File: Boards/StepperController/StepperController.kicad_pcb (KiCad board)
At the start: 2 copper layers, 160 x 100 mm, 167 parts, among them IC1 ATMEGA645A-A, J1 I2C, J2 SPI_Extern, J3 ISP, J4 Reference, J5 Display, J7 Spindle, P1 Power, P10 CONN_Z, P2 Cover, P3 USB_B, P4 Relay2, P5 Relay1, P6 Emer_Off, P8 CONN_X, P9 CONN_Y, Q1 BC817-40, Q2 BC817-40, Q3 BC817-40, Q4 BC817-40, Q5 BC817-40, SW2 SW_1, SW3 SW_2, U1 LM2595S-5, U2 74LS11, U3 FT232RL, U5 TMC2660, U6 TMC2660, U7 TMC2660, U8 74HC00, X1 16MHz, Y1 20MHz

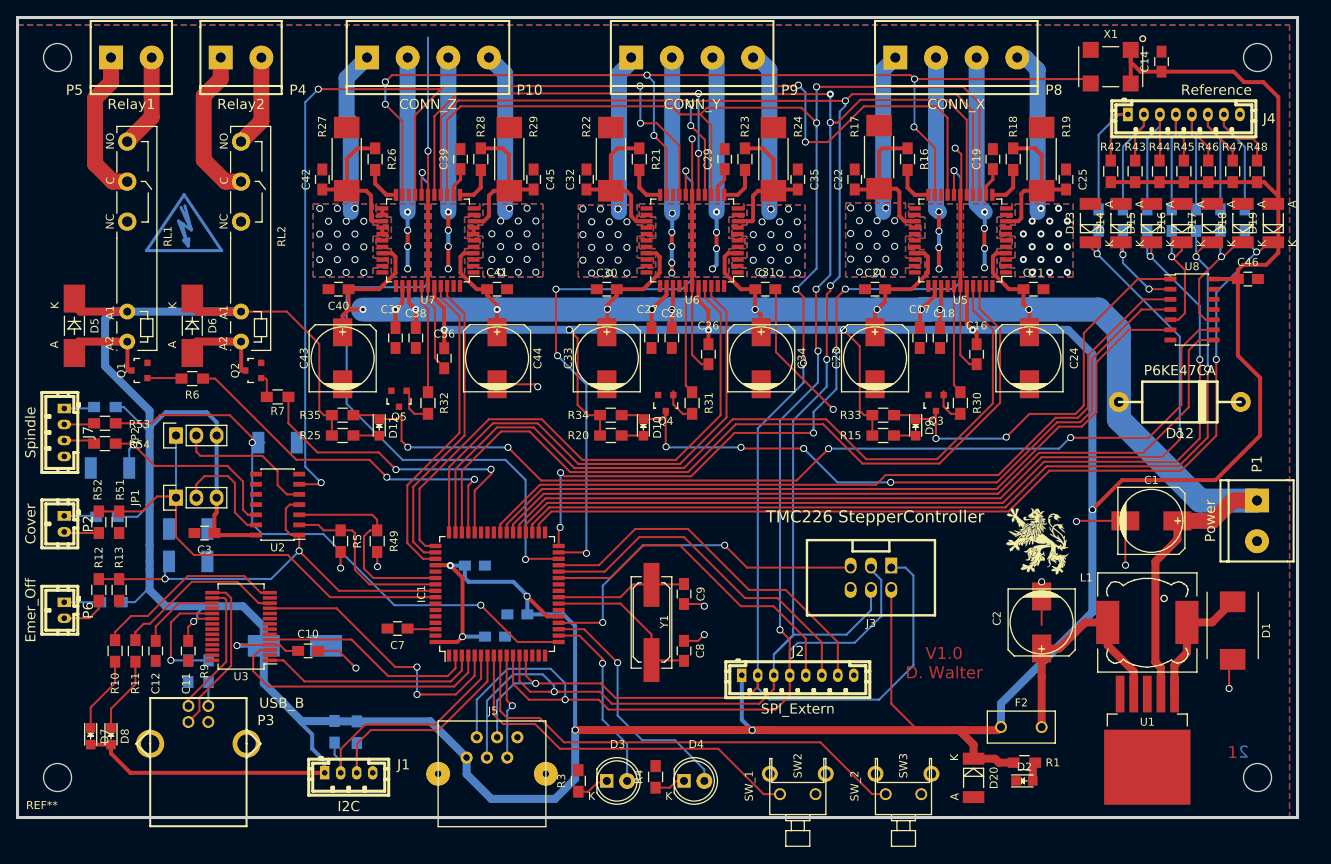
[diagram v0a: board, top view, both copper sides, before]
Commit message: Thermal vias, changed footprint of logic ics
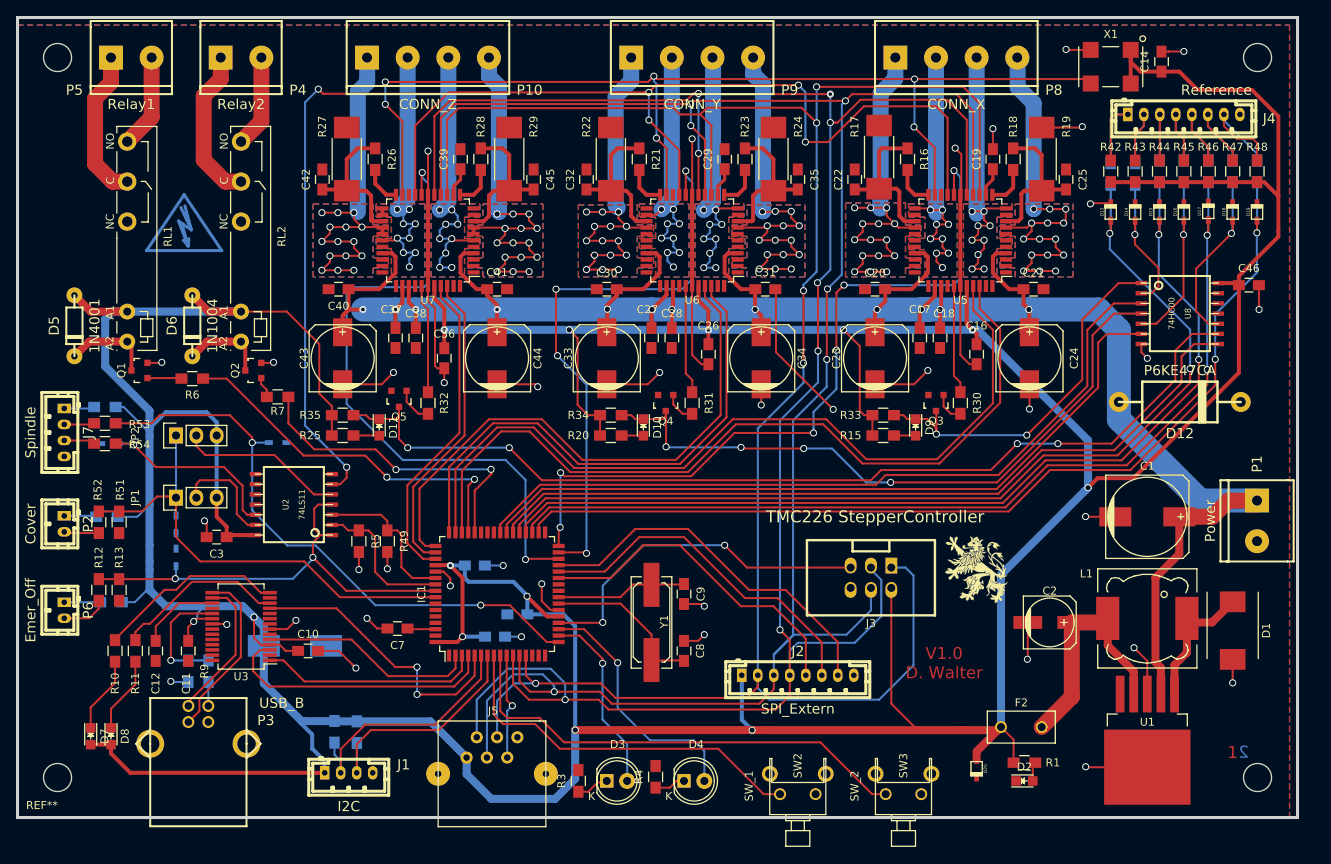
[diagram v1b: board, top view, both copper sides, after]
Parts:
- C1: footprint Capacitors_SMD:c_elec_8x10.5 -> Capacitors_SMD:c_elec_10x10.5
- C2: footprint Capacitors_SMD:c_elec_8x10.5 -> Capacitors_SMD:c_elec_6.3x5.7
- D13, D14, D15, D16, D17, D18, D19, D20, D21, D22, D23, D29: footprint Diodes_SMD:MELF_Standard -> w_smd_diode:sod323
- D5, D6: footprint Diodes_SMD:MELF_Handsoldering -> w_pth_diodes:diode_do35
- U2, U8: footprint Housings_SOIC:SOIC-14_3.9x8.7mm_Pitch1.27mm -> w_smd_dil:soic-14
- moved G*** 8.41 mm to (183.9, 121.9)
- moved R37 6.28 mm to (206.8, 72.1)
- moved R38 6.28 mm to (209.8, 72.1)
- moved R39 6.28 mm to (212.9, 72.1)
- moved R40 6.28 mm to (215.9, 72.1)
- moved R41 6.28 mm to (218.9, 72.1)
- moved R2 5.96 mm to (200.7, 72.5)
- moved R36 5.96 mm to (203.7, 72.5)
- moved D23 3.05 mm to (75.6, 106.2)
- moved D13 2.89 mm to (200.7, 77.2)
- moved D19 2.46 mm to (218.9, 77.2)
- moved R5 2.29 mm to (106.7, 118.4)
- moved D14 2.25 mm to (203.7, 77.2)
- moved U2 2.03 mm to (98.6, 113.8), turned to 90 degrees
- moved D18 1.88 mm to (215.9, 77.2)
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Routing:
- net /Controller/Stall_Z: track 15.7 -> 125.5 mm, vias 0 -> 4
- net GND: track 270.5 -> 231.2 mm, vias 18 -> 39
- net /Driver/Driver_Z/OA1_Z: track 21.0 -> 53.5 mm, vias 1 -> 15
- net /Driver/Driver_Y/OA1_Y: track 19.9 -> 52.0 mm, vias 1 -> 15
- net /Driver/Driver_X/OB1_X: track 20.2 -> 52.0 mm, vias 1 -> 15
- net /Driver/Driver_X/OA1_X: track 21.0 -> 52.3 mm, vias 1 -> 15
- net /Driver/Driver_Y/OB1_Y: track 20.6 -> 52.0 mm, vias 1 -> 15
- net /Driver/Driver_Z/OB1_Z: track 21.4 -> 52.0 mm, vias 1 -> 15
- net +5V: track 737.8 -> 715.2 mm
- net /Driver/Driver_Z/OA2_Z: track 26.4 -> 36.7 mm, vias 4 -> 9
- net /Driver/Driver_X/OA2_X: track 26.7 -> 36.9 mm, vias 4 -> 9
- net /Driver/Driver_Y/OA2_Y: track 26.6 -> 36.7 mm, vias 4 -> 9
- net /Driver/Driver_Z/OB2_Z: track 27.2 -> 36.7 mm, vias 4 -> 9
- net /Driver/Driver_X/OB2_X: track 26.6 -> 35.9 mm, vias 4 -> 9
- net /Driver/Driver_Y/OB2_Y: track 27.0 -> 36.2 mm, vias 5 -> 9
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
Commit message: Work in Progress
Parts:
- removed U8: 74HC00, w_smd_dil:soic-14
- added U4: 74HC08, w_smd_dil:so-14, F.Cu at (210.8, 89.9)
- C1: value 220µF -> 100µF; footprint Capacitors_SMD:c_elec_10x10.5 -> Capacitors_SMD:c_elec_8x10.5
- C2: value 100µF -> 1000µF; footprint Capacitors_SMD:c_elec_6.3x5.7 -> Capacitors_ThroughHole:C_Radial_D16_L25_P7.5
- D1: value MBRS240 -> SK34; footprint Diodes_SMD:DO-214AB -> w_smd_diode:do214ac
- D12: value P6KE47CA -> SM6T 39A; footprint w_pth_diodes:diode_do201 -> w_smd_diode:do214aa
- D13, D14, D16, D17, D18, D19: footprint w_smd_diode:sod323 -> w_smd_trans:sot23
- D15: value 5V -> ZMY5,6; footprint w_smd_diode:sod323 -> w_smd_trans:sot23
- D20: value 6V -> P6SMB 6,8A; footprint w_smd_diode:sod323 -> w_smd_diode:do214aa
- D21, D22, D23, D29: footprint w_smd_diode:sod323 -> w_smd_trans:sot23; moved to F.Cu
- D5: value 1N4001 -> 1N4148; footprint w_pth_diodes:diode_do35 -> w_smd_diode:sod323
- D6: value 1N1004 -> 1N4148; footprint w_pth_diodes:diode_do35 -> w_smd_diode:sod323
- U1: value LM2595S-5 -> LM2576S-5
- U2: value 74LS11 -> 74HC11; footprint w_smd_dil:soic-14 -> w_smd_dil:so-14
- moved G*** 34.6 mm to (149.4, 124.2)
- moved D22 22.3 mm to (74.9, 100.6), turned to 180 degrees
- moved C1 17.8 mm to (217.4, 128.3), turned to 180 degrees
- moved D12 14.7 mm to (210.8, 115.6), turned to 90 degrees
- moved D1 14.4 mm to (205.2, 119.9), turned to 180 degrees
- moved D2 8.19 mm to (182.4, 145.0), turned to 180 degrees
- moved R1 8.12 mm to (182.5, 142.7), turned to 180 degrees
- moved D20 7.41 mm to (190.8, 144.0), turned to 0 degrees
- moved C14 7.28 mm to (200.7, 54.9), turned to 180 degrees
- moved C8 4.68 mm to (142.7, 131.1)
- moved C9 4.64 mm to (142.7, 124.2)
- moved D23 4.61 mm to (79.4, 108.7)
- moved D29 4.47 mm to (79.4, 117.1), turned to 180 degrees
- moved C5 4.43 mm to (119.4, 129.3), turned to 90 degrees
- moved Y1 4.38 mm to (138.9, 127.8)
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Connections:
- C1 pad 1: /Driver/Sup_36V -> VSA
- C17 pad 1: /Driver/Sup_36V -> VSA
- C17 pad 2: GND -> Net-(C17-Pad2)
- C18 pad 1: /Driver/Sup_36V -> VSA
- C20 pad 1: /Driver/Sup_36V -> VSA
- C21 pad 1: /Driver/Sup_36V -> VSA
- C23 pad 1: /Driver/Sup_36V -> VSA
- C24 pad 1: /Driver/Sup_36V -> VSA
- C27 pad 1: /Driver/Sup_36V -> VSA
- C27 pad 2: GND -> Net-(C27-Pad2)
- C28 pad 1: /Driver/Sup_36V -> VSA
- C30 pad 1: /Driver/Sup_36V -> VSA
- C31 pad 1: /Driver/Sup_36V -> VSA
- C33 pad 1: /Driver/Sup_36V -> VSA
- C34 pad 1: /Driver/Sup_36V -> VSA
- C37 pad 1: /Driver/Sup_36V -> VSA
- C37 pad 2: GND -> Net-(C37-Pad2)
- C38 pad 1: /Driver/Sup_36V -> VSA
- C40 pad 1: /Driver/Sup_36V -> VSA
- C41 pad 1: /Driver/Sup_36V -> VSA
- C43 pad 1: /Driver/Sup_36V -> VSA
- C44 pad 1: /Driver/Sup_36V -> VSA
- D12 pad 1: /Driver/Sup_36V -> VSA
- P1 pad 1: /Driver/Sup_36V -> VSA
- U1 pad 1: Net-(D1-Pad1) -> VSA
- U1 pad 2: /Driver/Sup_36V -> Net-(D1-Pad1)
- U5 pad 1: (no net) -> VSA
- U5 pad 30: /Driver/Sup_36V -> VSA
- U5 pad 33: (no net) -> VSA
- U5 pad 35: /Driver/Sup_36V -> Net-(C17-Pad2)
- U5 pad 36: /Driver/Sup_36V -> VSA
- U5 pad 4: /Driver/Sup_36V -> VSA
- U6 pad 1: (no net) -> VSA
- U6 pad 30: /Driver/Sup_36V -> VSA
- U6 pad 33: (no net) -> VSA
- U6 pad 35: /Driver/Sup_36V -> Net-(C27-Pad2)
- U6 pad 36: /Driver/Sup_36V -> VSA
- U6 pad 4: /Driver/Sup_36V -> VSA
- U7 pad 1: (no net) -> VSA
- U7 pad 30: /Driver/Sup_36V -> VSA
- U7 pad 33: (no net) -> VSA
- U7 pad 35: /Driver/Sup_36V -> Net-(C37-Pad2)
- U7 pad 36: /Driver/Sup_36V -> VSA
- U7 pad 4: /Driver/Sup_36V -> VSA
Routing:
- net /Driver/Sup_36V: track 295.7 -> 0.00 mm, vias 12 -> 0
- net VSA: track 0.00 -> 211.4 mm
- net /Driver/Driver_X/OA1_X: track 52.3 -> 25.1 mm, vias 15 -> 1
- net /Driver/Driver_X/BRB_X: track 20.7 -> 0.00 mm
- net /Driver/Driver_X/BRA_X: track 19.5 -> 0.00 mm
- net /Driver/Driver_X/OB1_X: track 52.0 -> 36.1 mm, vias 15 -> 6
- net GND: track 231.2 -> 218.1 mm, vias 39 -> 55
- net /Controller/Step_X: track 102.4 -> 94.5 mm
- net /Controller/Dir_X: track 102.5 -> 95.0 mm
- net Net-(D1-Pad1): track 16.4 -> 22.8 mm
- net /Controller/Rel_2: track 39.8 -> 33.4 mm
- net /Driver/Driver_X/SRB_X: track 5.18 -> 0.00 mm
- net /Driver/Driver_X/SRA_X: track 5.18 -> 0.00 mm
- net Net-(C8-Pad1): track 20.5 -> 15.5 mm
- net Net-(C2-Pad1): track 29.4 -> 34.4 mm
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- added copper zone on F.Cu, net /Driver/Driver_X/BRA_X
- added copper zone on F.Cu, net /Driver/Driver_X/BRB_X
- added copper zone on F.Cu, net /Driver/Driver_X/SRA_X
- added copper zone on F.Cu, net /Driver/Driver_X/SRB_X
- added copper zone on F.Cu, net VSA
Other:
- board text added: "Display"
- board text added: "ISP"
- board text added: "TMC2660 StepperController"
- board text removed: "TMC226 StepperController"

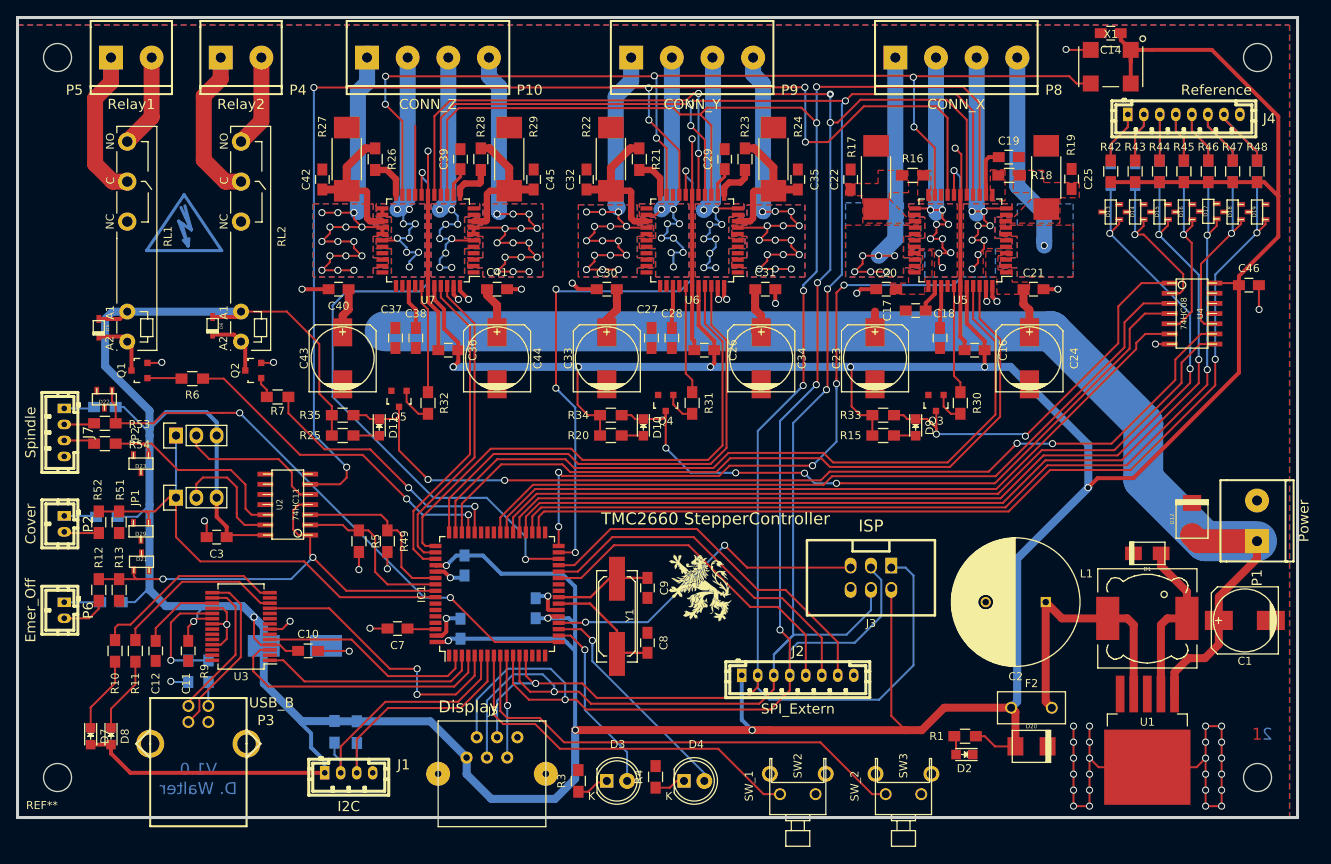
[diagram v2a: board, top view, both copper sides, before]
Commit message: Added Ext. Connector, new Layout of Supply to TMC2660
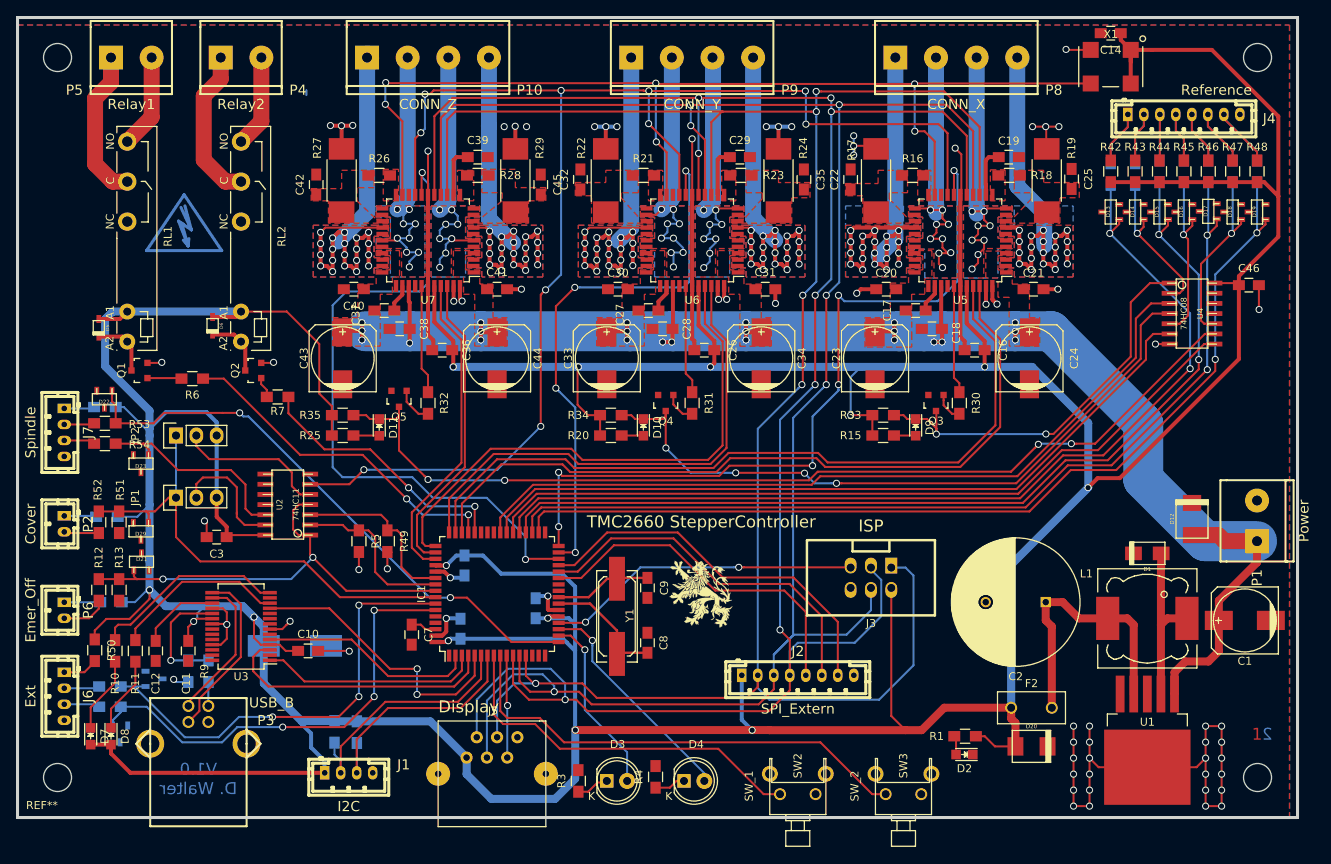
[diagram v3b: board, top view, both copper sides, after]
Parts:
- added D24: ZMY5,6, w_smd_trans:sot23, B.Cu at (81.1, 135.6)
- added D25: ZMY5,6, w_smd_trans:sot23, B.Cu at (76.8, 142.5)
- added J6: Ext, w_conn_jst-ph:b4b-ph-kl, F.Cu at (69.8, 137.7)
- added R50: 10R, Resistors_SMD:R_0805_HandSoldering, F.Cu at (73.7, 132.0)
- added R55: 10R, Resistors_SMD:R_0805_HandSoldering, B.Cu at (75.6, 136.5)
- added R60: 10R, Resistors_SMD:R_0805_HandSoldering, B.Cu at (75.6, 139.1)
- R12, R14, R52, R53, R54, R58, R59: value 100R -> 10R
- moved C37 3.70 mm to (109.9, 89.5), turned to 0 degrees
- moved C27 3.45 mm to (142.9, 89.5), turned to 0 degrees
- moved R29 2.77 mm to (126.2, 73.3)
- moved R27 2.74 mm to (104.5, 73.3)
- moved R22 2.74 mm to (137.5, 73.3)
- moved R24 2.74 mm to (159.1, 73.3)
- moved C38 2.31 mm to (111.8, 91.8), turned to 180 degrees
- moved C39 2.17 mm to (121.5, 70.4), turned to 0 degrees
- moved R21 2.09 mm to (142.2, 72.6), turned to 0 degrees
- moved R23 2.09 mm to (154.4, 72.6), turned to 180 degrees
- moved R26 2.09 mm to (109.2, 72.6), turned to 0 degrees
- moved R28 2.07 mm to (121.5, 72.6), turned to 180 degrees
- moved C7 1.93 mm to (113.3, 130.0), turned to 270 degrees
- moved C29 1.92 mm to (154.3, 70.4), turned to 0 degrees
- moved C40 1.91 mm to (106.0, 86.9)
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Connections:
- IC1 pad 58: (no net) -> /Controller/Ext1
- IC1 pad 59: (no net) -> /Controller/Ext2
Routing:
- net /Controller/Ext2: track 0.00 -> 57.2 mm, vias 0 -> 3
- net /Controller/Ext1: track 0.00 -> 57.0 mm, vias 0 -> 3
- net /Driver/Driver_X/OA1_X: track 25.1 -> 55.0 mm, vias 1 -> 20
- net /Driver/Driver_X/OB1_X: track 36.1 -> 62.9 mm, vias 6 -> 20
- net GND: track 218.1 -> 239.4 mm, vias 55 -> 68
- net /Driver/Driver_Z/BRB_Z: track 18.8 -> 0.00 mm
- net /Driver/Driver_Y/BRA_Y: track 18.8 -> 0.00 mm
- net /Driver/Driver_Y/BRB_Y: track 18.7 -> 0.00 mm
- net /Driver/Driver_Z/BRA_Z: track 18.7 -> 0.00 mm
- net +5V: track 712.8 -> 725.0 mm, vias 13 -> 14
- net /Driver/Driver_Y/OB1_Y: track 51.1 -> 61.0 mm, vias 15 -> 20
- net /Driver/Driver_Z/OB1_Z: track 52.0 -> 61.5 mm, vias 15 -> 20
- net VSA: track 211.4 -> 217.9 mm, vias 0 -> 23
- net /Driver/Driver_Z/SRA_Z: track 5.29 -> 0.00 mm
- net /Controller/CS_Z: track 79.9 -> 85.0 mm
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- added copper zone on F.Cu, net /Driver/Driver_Y/BRA_Y
- added copper zone on F.Cu, net /Driver/Driver_Y/BRB_Y
- added copper zone on F.Cu, net /Driver/Driver_Y/SRA_Y
- added copper zone on F.Cu, net /Driver/Driver_Y/SRB_Y
- added copper zone on F.Cu, net /Driver/Driver_Z/BRA_Z
- added copper zone on F.Cu, net /Driver/Driver_Z/BRB_Z
- added copper zone on F.Cu, net /Driver/Driver_Z/SRA_Z
- added copper zone on F.Cu, net /Driver/Driver_Z/SRB_Z

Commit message: Layout updated
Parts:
- added C15: 10µF, Capacitors_SMD:C_0805_HandSoldering, B.Cu at (186.1, 123.8)
- added C47: 10µF, Capacitors_SMD:C_0805_HandSoldering, B.Cu at (125.1, 123.8)
- C13: footprint Capacitors_Tantalum_SMD:TantalC_SizeD_EIA-7343_HandSoldering -> Capacitors_SMD:C_0805_HandSoldering
- D12: value SM6T 39A -> SM6T 30CA
- L1: value 100µH -> L-PISR 100µH; footprint Choke_SMD:Choke_SMD_12x12mm_h8mm -> Choke_SMD:Choke_SMD_PISR_Handsoldering_FASTRON
- moved D1 11.0 mm to (206.4, 130.8)
- moved L1 7.38 mm to (205.7, 120.7), turned to 0 degrees
- moved D8 6.32 mm to (78.1, 148.6)
- moved D7 6.11 mm to (74.9, 148.6)
- moved P1 5.97 mm to (218.9, 109.9)
- moved D12 5.74 mm to (210.8, 109.9)
- moved C14 5.46 mm to (200.7, 60.3), turned to 90 degrees
- moved X1 4.81 mm to (196.0, 60.3), turned to 90 degrees
- moved C2 3.43 mm to (189.9, 123.8)
- moved C1 3.30 mm to (216.5, 131.4)
- moved J3 3.05 mm to (167.6, 122.9)
- moved C13 2.18 mm to (96.5, 131.4)
- moved R2 0.33 mm to (200.7, 72.1)
- moved R36 0.33 mm to (203.7, 72.1)
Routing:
- net /Controller/SDO: track 257.0 -> 233.8 mm, vias 5 -> 6
- net Net-(C15-Pad1): track 34.4 -> 51.2 mm
- net Net-(D7-Pad1): track 9.53 -> 14.6 mm
- net +5V: track 725.0 -> 720.0 mm
- net Net-(D8-Pad1): track 9.53 -> 14.4 mm
- net /Controller/SDI: track 247.0 -> 243.1 mm
- net Net-(IC1-Pad20): track 39.6 -> 36.5 mm
- net Net-(J4-Pad7): track 15.0 -> 16.8 mm
- net /Controller/SCK: track 258.9 -> 257.1 mm
- net /Driver/Driver_X/TMC_Clock: track 133.3 -> 131.8 mm
- net VSA: track 217.9 -> 216.6 mm
- net GND: track 239.4 -> 238.8 mm, vias 68 -> 67
- net (no net): vias 2 -> 0

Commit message: Pre-Release Layout
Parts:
- added D26: LED, LEDs:LED_0805, F.Cu at (69.1, 111.8)
- added D27: LED, LEDs:LED_0805, F.Cu at (69.1, 122.4)
- added D28: LED, LEDs:LED_0805, F.Cu at (69.1, 98.0)
- added D30: LED, LEDs:LED_0805, F.Cu at (71.1, 91.4)
- added D31: LED, LEDs:LED_0805, F.Cu at (85.3, 91.4)
- added Q6: BC807-40, TO_SOT_Packages_SMD:SOT-23, B.Cu at (74.2, 111.5)
- added Q7: BC807-40, TO_SOT_Packages_SMD:SOT-23, B.Cu at (74.2, 121.4)
- added Q8: BC817-40, TO_SOT_Packages_SMD:SOT-23, B.Cu at (69.1, 94.0)
- added R61: 270R, Resistors_SMD:R_0805_HandSoldering, B.Cu at (69.1, 111.8)
- added R62: 270R, Resistors_SMD:R_0805_HandSoldering, B.Cu at (69.1, 98.0)
- added R63: 270R, Resistors_SMD:R_0805_HandSoldering, B.Cu at (69.1, 122.4)
- added R64: 270R, Resistors_SMD:R_0805_HandSoldering, F.Cu at (72.6, 87.9)
- added R65: 1k, Resistors_SMD:R_0805_HandSoldering, B.Cu at (97.5, 114.8)
- added R66: 270R, Resistors_SMD:R_0805_HandSoldering, F.Cu at (87.0, 87.9)
- R12, R14: value 10R -> 100R
- R6, R7: value 10k -> 1k
- moved C28 1.81 mm to (145.9, 93.1), turned to 270 degrees
- moved C18 1.71 mm to (179.5, 93.1), turned to 270 degrees
- moved C38 1.70 mm to (112.9, 93.1), turned to 270 degrees
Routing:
- net Net-(Q8-Pad1): track 0.00 -> 38.5 mm, vias 0 -> 2
- net +5V: track 720.0 -> 743.3 mm
- net /Interface/Spindle_Enable: track 21.3 -> 27.2 mm, vias 0 -> 1
- net VSA: track 216.6 -> 222.4 mm, vias 23 -> 18
- net Net-(D28-Pad1): track 0.00 -> 5.59 mm, vias 0 -> 1
- net Net-(Q7-Pad2): track 0.00 -> 4.13 mm
- net Net-(D28-Pad2): track 0.00 -> 3.57 mm, vias 0 -> 1
- net Net-(D26-Pad2): track 0.00 -> 3.56 mm, vias 0 -> 1
- net /Controller/SDI: track 243.1 -> 239.6 mm
- net /Controller/Emergency_Off: track 56.5 -> 59.9 mm, vias 2 -> 3
- net /Controller/Cover: track 60.5 -> 63.8 mm, vias 0 -> 1
- net Net-(Q6-Pad2): track 0.00 -> 3.23 mm
- net Net-(D27-Pad2): track 0.00 -> 3.18 mm, vias 0 -> 1
- net Net-(D30-Pad1): track 7.67 -> 10.8 mm
- net Net-(D31-Pad2): track 0.00 -> 3.14 mm
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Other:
- board text added: "5V OK"
- board text added: "RX TX"
- board text added: "Stall X"
- board text added: "Stall Y"
- board text added: "Stall Z"
